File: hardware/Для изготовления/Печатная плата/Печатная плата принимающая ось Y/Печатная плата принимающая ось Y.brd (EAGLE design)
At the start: 60.4 x 38.1 mm, 10 parts, among them J1 22-03-5035

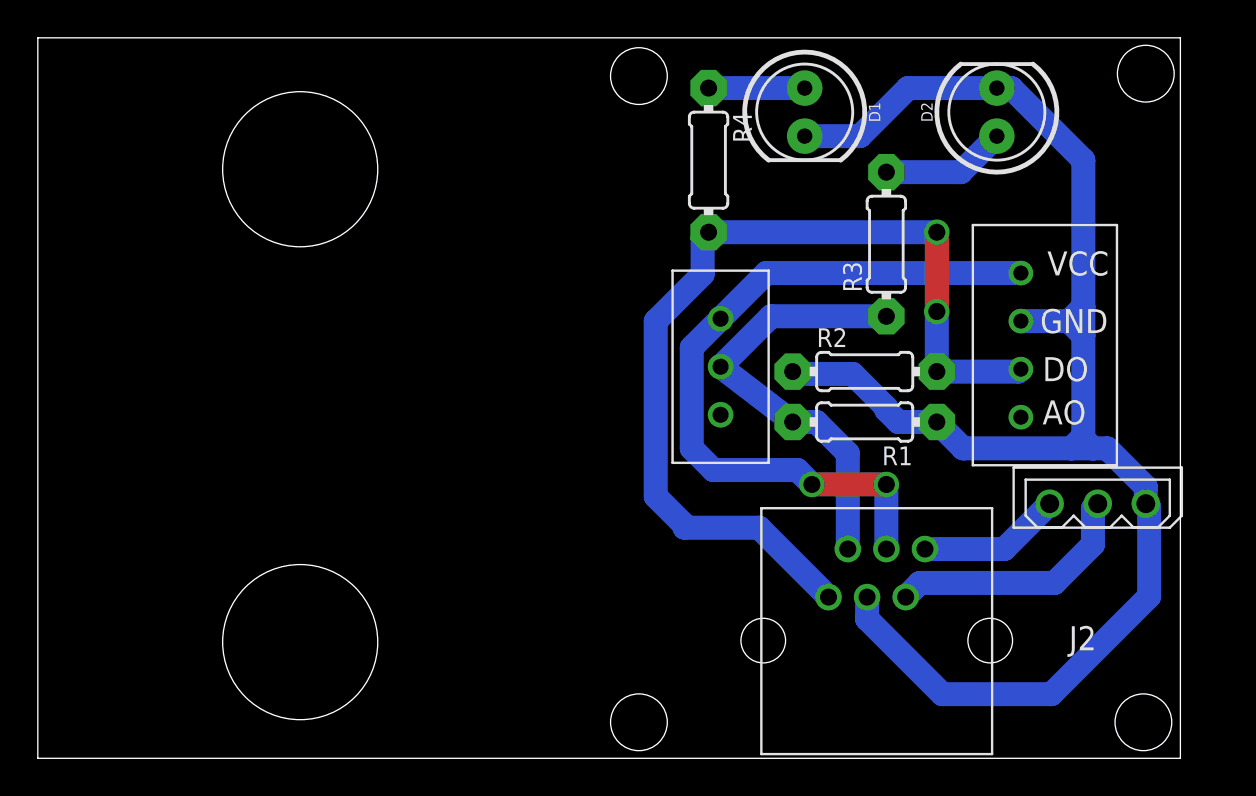
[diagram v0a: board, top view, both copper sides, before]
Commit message: принимающие платы разделены по осям
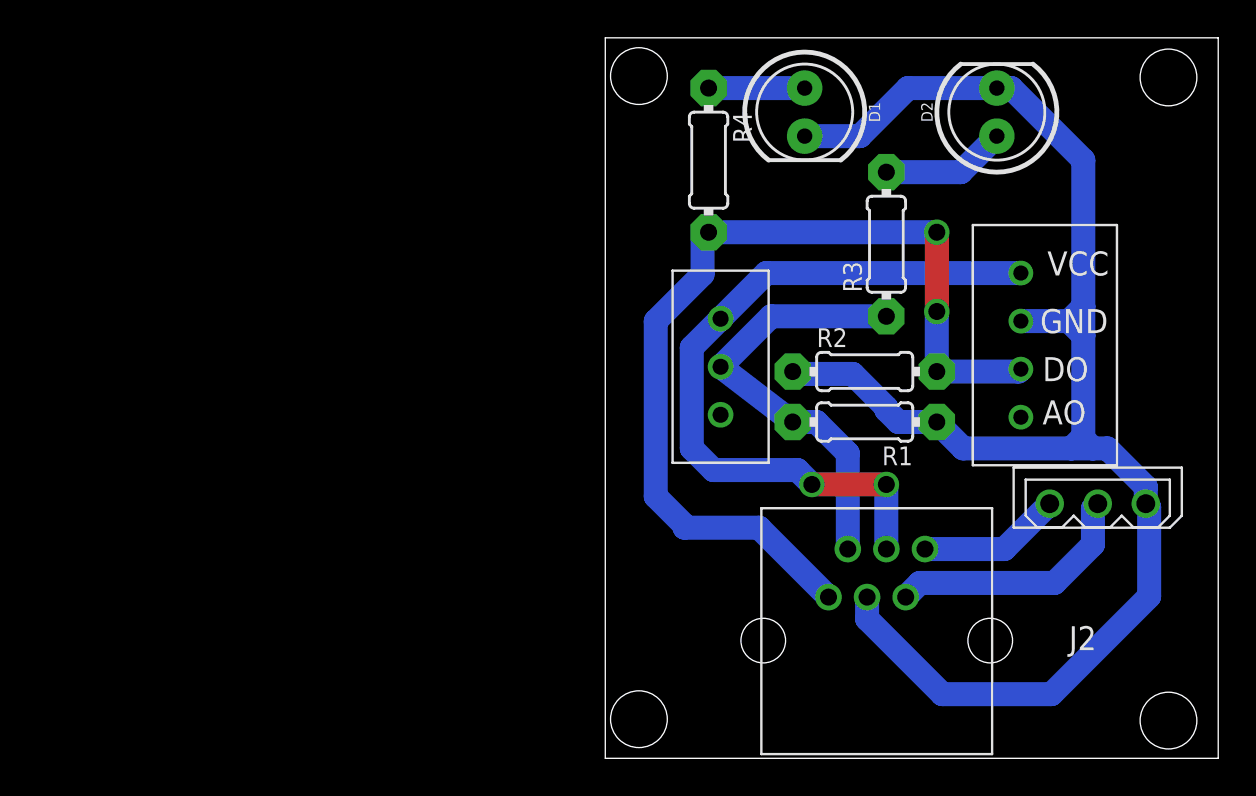
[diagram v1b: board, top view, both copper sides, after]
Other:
- board size 60.4 x 38.1 mm -> 32.4 x 38.1 mm
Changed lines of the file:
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@@
 <setting verticaltext="up"/>
 </settings>
-<grid distance="10" unitdist="mm" unit="mm" style="lines" multiple="1" display="no" altdistance="5" altunitdist="mm" altunit="mm"/>
+<grid distance="1" unitdist="mm" unit="mm" style="lines" multiple="1" display="no" altdistance="0.1" altunitdist="mm" altunit="mm"/>
 <layers>
 <layer number="1" name="Top" color="4" fill="1" visible="yes" active="yes"/>
@@
 <board>
 <plain>
-<wire x1="-13.871" y1="-1.143" x2="46.533" y2="-1.143" width="0" layer="20"/>
-<wire x1="46.533" y1="-1.143" x2="46.533" y2="36.947" width="0" layer="20"/>
-<wire x1="46.533" y1="36.947" x2="-13.871" y2="36.947" width="0" layer="20"/>
-<wire x1="-13.871" y1="36.947" x2="-13.871" y2="-1.143" width="0" layer="20"/>
+<wire x1="16.129" y1="-1.143" x2="48.533" y2="-1.143" width="0" layer="20"/>
+<wire x1="48.533" y1="-1.143" x2="48.533" y2="36.947" width="0" layer="20"/>
+<wire x1="48.533" y1="36.947" x2="16.129" y2="36.947" width="0" layer="20"/>
+<wire x1="16.129" y1="36.947" x2="16.129" y2="-1.143" width="0" layer="20"/>
 <hole x="17.907" y="34.925" drill="3"/>
-<hole x="17.907" y="0.762" drill="3"/>
-<hole x="44.577" y="0.762" drill="3"/>
-<hole x="44.704" y="35.052" drill="3"/>
-<hole x="0" y="30" drill="8.2"/>
-<hole x="0" y="5" drill="8.2"/>
+<hole x="45.904" y="34.852" drill="3"/>
+<hole x="17.907" y="0.925" drill="3"/>
+<hole x="45.904" y="0.852" drill="3"/>
 </plain>
 <attributes>
